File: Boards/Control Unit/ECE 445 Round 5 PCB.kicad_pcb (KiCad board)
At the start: 2 copper layers, 92.1 x 90 mm, 48 parts, among them J1 Screw_Terminal_01x12, J10 Screw_Terminal_01x03, J11 Screw_Terminal_01x12, J12 Screw_Terminal_01x03, J13 Screw_Terminal_01x03, J14 Screw_Terminal_01x03, J15 Screw_Terminal_01x03, J16 Screw_Terminal_01x03, J17 Screw_Terminal_01x03, J18 Screw_Terminal_01x03, J19 Screw_Terminal_01x03, J20 Conn_ARM_JTAG_SWD_10, J27 Screw_Terminal_01x12, J28 Screw_Terminal_01x12, J3 Screw_Terminal_01x03, J4 Screw_Terminal_01x03, J5 Screw_Terminal_01x03, J6 Screw_Terminal_01x03, J7 Conn_02x03_Odd_Even, J9 Screw_Terminal_01x03, Q1 NMOS, Q10 NMOS, Q11 NMOS, Q12 NMOS, Q2 NMOS, Q3 NMOS, Q4 NMOS, Q5 NMOS, Q6 NMOS, Q7 NMOS, Q8 NMOS, Q9 NMOS, SW1 SW_Push, U1 STM32F401RBTx

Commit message: Add files via upload
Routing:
- net /Radar_Read: track 0.00 -> 20.4 mm, vias 0 -> 2
- net /H4: track 50.3 -> 44.1 mm, vias 0 -> 2
- net /bigmotor: track 0.00 -> 3.10 mm, vias 0 -> 1
- net /H7: track 17.3 -> 18.0 mm
- net /H8: track 19.2 -> 20.0 mm
- net /JTDI: track 23.7 -> 24.5 mm

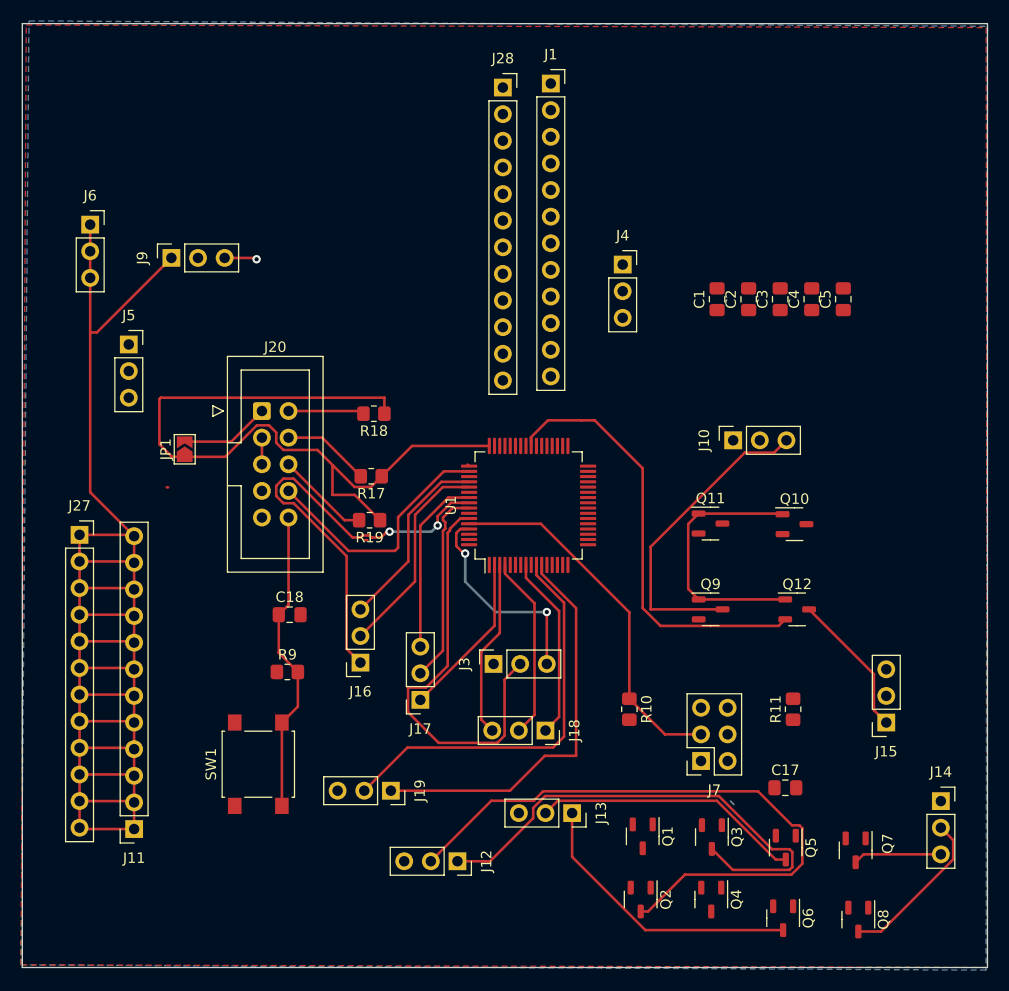
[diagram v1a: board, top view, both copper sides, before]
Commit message: removed extranious 5v power buses
hall effect module is pretty nice
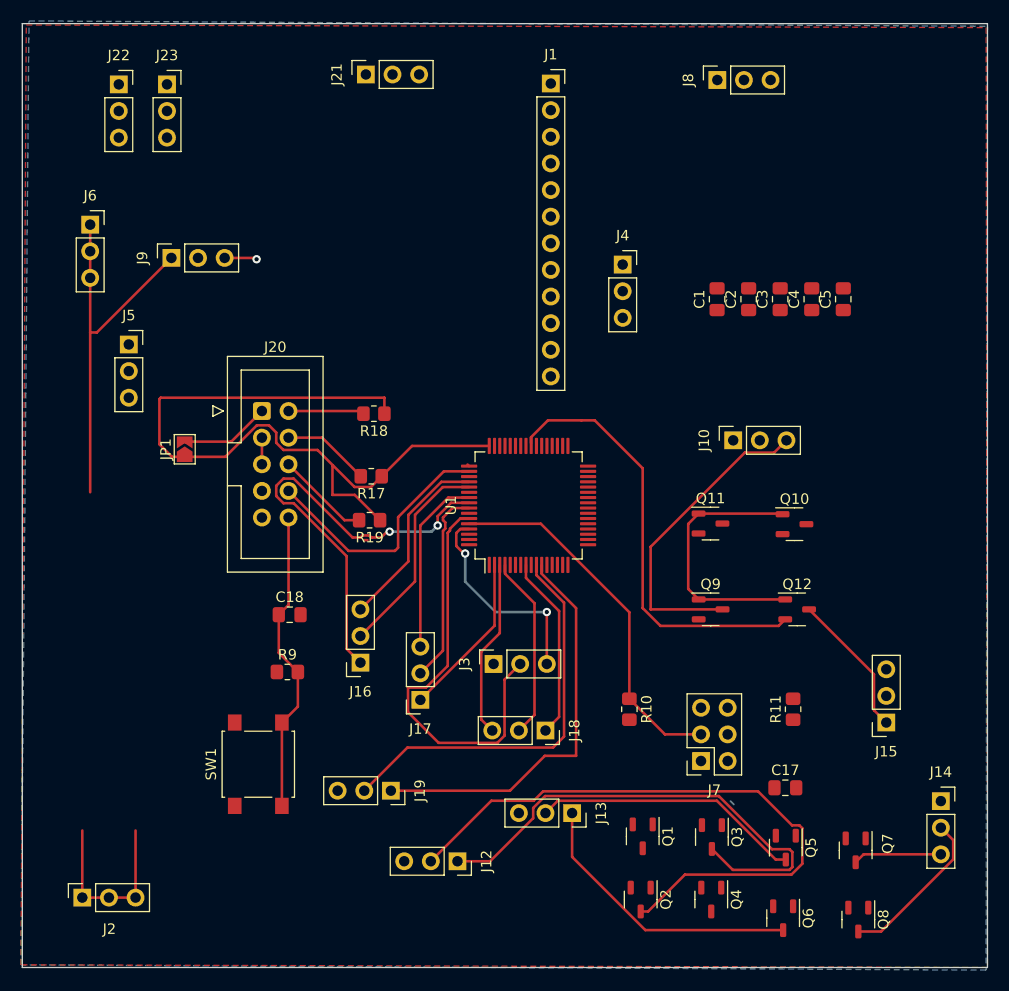
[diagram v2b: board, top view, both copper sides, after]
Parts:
- removed J11, J27, J28: Screw_Terminal_01x12, Connector_PinSocket_2.54mm:PinSocket_1x12_P2.54mm_Vertical
- added J2: Screw_Terminal_01x03, Connector_PinSocket_2.54mm:PinSocket_1x03_P2.54mm_Vertical, F.Cu at (105.4, 123.0)
- added J21: Screw_Terminal_01x03, Connector_PinSocket_2.54mm:PinSocket_1x03_P2.54mm_Vertical, F.Cu at (132.5, 44.5)
- added J22: Screw_Terminal_01x03, Connector_PinSocket_2.54mm:PinSocket_1x03_P2.54mm_Vertical, F.Cu at (108.9, 45.4)
- added J23: Screw_Terminal_01x03, Connector_PinSocket_2.54mm:PinSocket_1x03_P2.54mm_Vertical, F.Cu at (113.5, 45.4)
- added J8: Screw_Terminal_01x03, Connector_PinSocket_2.54mm:PinSocket_1x03_P2.54mm_Vertical, F.Cu at (166.0, 45.0)
- C18: value 1u -> 1uF
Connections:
- U1 pad 40: /T11 -> unconnected-(U1-PC9-Pad40)
- U1 pad 44: /D- -> /T11
- U1 pad 45: /D+ -> unconnected-(U1-PA12-Pad45)
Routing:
- net +5V: track 161.1 -> 54.1 mm

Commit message: routed except gnd and vcc
that was rough
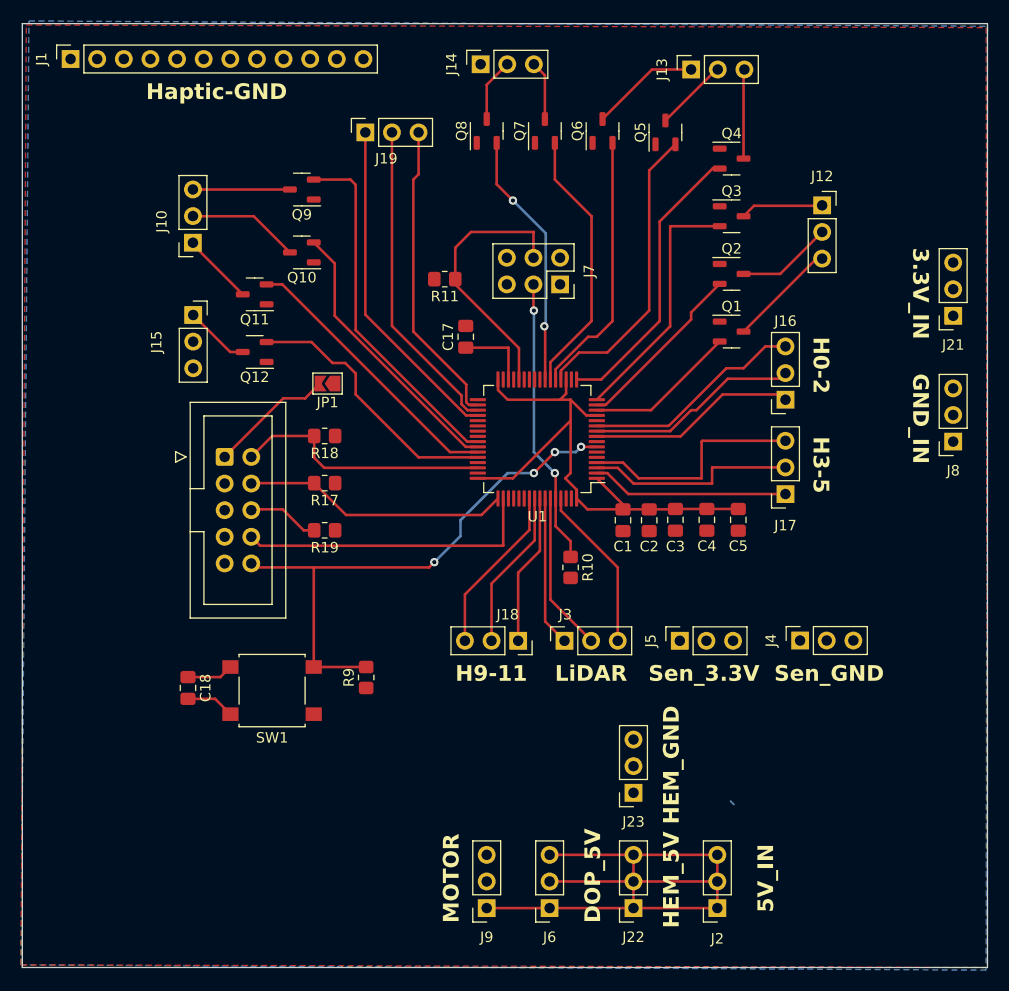
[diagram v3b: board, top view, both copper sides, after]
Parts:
- moved J22 92.7 mm to (158.0, 124.0), turned to 180 degrees
- moved Q8 83.2 mm to (144.0, 49.9), turned to 90 degrees
- moved J14 82.9 mm to (143.4, 43.5), turned to 90 degrees
- moved J23 80.9 mm to (158.0, 113.0), turned to 180 degrees
- moved J6 78.6 mm to (150.0, 124.0), turned to 180 degrees
- moved Q6 77.1 mm to (155.1, 49.9), turned to 90 degrees
- moved J15 76.7 mm to (116.0, 67.4), turned to 0 degrees
- moved Q7 74.8 mm to (149.6, 49.9), turned to 90 degrees
- moved J13 71.8 mm to (163.5, 44.0), turned to 90 degrees
- moved J12 71.6 mm to (176.0, 57.0), turned to 0 degrees
- moved Q4 70.7 mm to (167.4, 52.5), turned to 0 degrees
- moved Q5 69.2 mm to (161.1, 50.0), turned to 90 degrees
- moved J9 68.9 mm to (144.0, 124.0), turned to 180 degrees
- moved J19 62.8 mm to (132.4, 50.0), turned to 90 degrees
- moved J2 60.6 mm to (166.0, 124.0), turned to 180 degrees
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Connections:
- J16 pad 1: /H4 -> /H2
- J16 pad 2: /H8 -> /H1
- J16 pad 3: /H7 -> /H0
- J17 pad 1: /H10 -> /H5
- J17 pad 2: /H5 -> /H4
- J17 pad 3: /H6 -> /H3
- J18 pad 1: /H0 -> /H11
- J18 pad 2: /H9 -> /H10
- J18 pad 3: /H11 -> /H9
- J19 pad 1: /H3 -> /H8
- J19 pad 2: /H2 -> /H7
- J19 pad 3: /H1 -> /H6
- U1 pad 10: /H2 -> /H1
- U1 pad 11: /H3 -> /H0
- U1 pad 2: /H10 -> /H5
- U1 pad 3: /H11 -> /H4
- U1 pad 34: unconnected-(U1-PB13-Pad34) -> /H6
- U1 pad 35: unconnected-(U1-PB14-Pad35) -> /H7
- U1 pad 36: unconnected-(U1-PB15-Pad36) -> /H8
- U1 pad 4: /H9 -> /H3
- U1 pad 52: /H7 -> unconnected-(U1-PC11-Pad52)
- U1 pad 53: /H8 -> unconnected-(U1-PC12-Pad53)
- U1 pad 55: /H6 -> /H9
- U1 pad 56: /H4 -> /H10
- U1 pad 57: /H5 -> /H11
- U1 pad 8: /H0 -> unconnected-(U1-PC0-Pad8)
- U1 pad 9: /H1 -> /H2
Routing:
- net /M1: track 60.4 -> 9.16 mm
- net +3.3V: track 99.3 -> 55.1 mm
- net /M2: track 47.4 -> 7.93 mm
- net /T8: track 0.00 -> 34.1 mm
- net /T4: track 0.00 -> 28.5 mm
- net /NRST: track 29.3 -> 57.7 mm, vias 0 -> 4
- net /T3: track 0.00 -> 27.6 mm
- net /T10: track 0.00 -> 26.8 mm
- net /T9: track 0.00 -> 26.7 mm
- net BOOT1: track 0.00 -> 25.7 mm
- net /T6: track 0.00 -> 25.7 mm
- net /I2C1_SDA: track 40.5 -> 15.2 mm
- net /T5: track 0.00 -> 25.3 mm
- net /T7: track 0.00 -> 24.6 mm, vias 0 -> 2
- net /T2: track 0.00 -> 24.1 mm
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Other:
- board text added: "3.3V_IN"
- board text added: "5V_IN"
- board text added: "DOP_5V"
- board text added: "GND_IN"
- board text added: "H0-2"
- board text added: "H3-5"
- board text added: "H9-11"
- board text added: "HEM_5V"
- board text added: "HEM_GND"
- board text added: "Haptic-GND"
- board text added: "LiDAR"
- board text added: "MOTOR"
- board text added: "Sen_3.3V"
- board text added: "Sen_GND"

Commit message: power routing example
oop
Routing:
- net +3.3V: track 55.1 -> 147.0 mm, vias 0 -> 4
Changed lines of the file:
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@@
     (property "ki_keywords" "transistor NMOS N-MOS N-MOSFET simulation")
     (attr smd)
-    (fp_text reference "Q2" (at 0 -2.4) (layer "F.SilkS")
+    (fp_text reference "Q2" (at -3.3625 -0.5) (layer "F.SilkS")
         (effects (font (size 1 1) (thickness 0.15)))
     )
@@
     (property "ki_keywords" "transistor NMOS N-MOS N-MOSFET simulation")
     (attr smd)
-    (fp_text reference "Q1" (at 0 -2.4) (layer "F.SilkS")
+    (fp_text reference "Q1" (at -3.3625 0) (layer "F.SilkS")
         (effects (font (size 1 1) (thickness 0.15)))
     )
@@
   (segment (start 157 85.9625) (end 153.6125 85.9625) (width 0.25) (layer "F.Cu") (net 3))
   (segment (start 146 75.5) (end 151 75.5) (width 0.25) (layer "F.Cu") (net 3))
+  (segment (start 179.5 87.5) (end 176.575 90.425) (width 0.25) (layer "F.Cu") (net 3))
   (segment (start 153.6125 85.9625) (end 152.575 84.925) (width 0.25) (layer "F.Cu") (net 3))
   (segment (start 151 75.5) (end 152 75.5) (width 0.25) (layer "F.Cu") (net 3))
   (segment (start 162 85.925) (end 165 85.925) (width 0.25) (layer "F.Cu") (net 3))
+  (segment (start 172.5 90.425) (end 168 85.925) (width 0.25) (layer "F.Cu") (net 3))
+  (segment (start 177.5 66.5) (end 173.5 66.5) (width 0.25) (layer "F.Cu") (net 3))
   (segment (start 157 85.9625) (end 159.5 85.9625) (width 0.25) (layer "F.Cu") (net 3))
   (segment (start 151.492764 83) (end 152 82.492764) (width 0.25) (layer "F.Cu") (net 3))
+  (segment (start 167 61) (end 167 61.775) (width 0.25) (layer "F.Cu") (net 3))
   (segment (start 151 75.5) (end 151.575 74.925) (width 0.25) (layer "F.Cu") (net 3))
+  (segment (start 181.58 62.42) (end 177.5 66.5) (width 0.25) (layer "F.Cu") (net 3))
   (segment (start 152 82.492764) (end 152 75.5) (width 0.25) (layer "F.Cu") (net 3))
+  (segment (start 176.575 90.425) (end 172.5 90.425) (width 0.25) (layer "F.Cu") (net 3))
+  (segment (start 181.58 62.42) (end 181.58 60) (width 0.75) (layer "F.Cu") (net 3))
   (segment (start 161.9625 85.9625) (end 162 85.925) (width 0.25) (layer "F.Cu") (net 3))
+  (segment (start 181.58 60) (end 181.58 56.08) (width 0.75) (layer "F.Cu") (net 3))
   (segment (start 157 85.5) (end 154.5 83) (width 0.25) (layer "F.Cu") (net 3))
+  (segment (start 181.58 56.08) (end 178 52.5) (width 0.75) (layer "F.Cu") (net 3))
+  (segment (start 167 61.775) (end 166.225 62.55) (width 0.25) (layer "F.Cu") (net 3))
   (segment (start 165 85.925) (end 168 85.925) (width 0.25) (layer "F.Cu") (net 3))
   (segment (start 145.075 74.575) (end 146 75.5) (width 0.25) (layer "F.Cu") (net 3))
   (segment (start 153.5 77) (end 154.5 77) (width 0.25) (layer "F.Cu") (net 3))
+  (segment (start 166.5 67.775) (end 166.225 68.05) (width 0.25) (layer "F.Cu") (net 3))
+  (segment (start 179.5 76.5) (end 179.5 87.5) (width 0.25) (layer "F.Cu") (net 3))
+  (segment (start 181.58 60) (end 179.5 60) (width 0.25) (layer "F.Cu") (net 3))
   (segment (start 146.5 83) (end 152 77.5) (width 0.25) (layer "F.Cu") (net 3))
+  (segment (start 188.5 62.42) (end 181.58 62.42) (width 0.75) (layer "F.Cu") (net 3))
+  (segment (start 188.5 67.5) (end 179.5 76.5) (width 0.25) (layer "F.Cu") (net 3))
   (segment (start 143.15 83) (end 146.5 83) (width 0.25) (layer "F.Cu") (net 3))
+  (segment (start 166.5 66.5) (end 166.5 67.775) (width 0.25) (layer "F.Cu") (net 3))
   (segment (start 145.075 73.575) (end 145.075 74.575) (width 0.25) (layer "F.Cu") (net 3))
   (segment (start 159.5 85.9625) (end 161.9625 85.9625) (width 0.25) (layer "F.Cu") (net 3))
   (segment (start 157 85.9625) (end 157 85.5) (width 0.25) (layer "F.Cu") (net 3))
   (segment (start 152.575 84.082236) (end 152.575 84.925) (width 0.25) (layer "F.Cu") (net 3))
+  (via (at 167 61) (size 0.8) (drill 0.4) (layers "F.Cu" "B.Cu") (net 3))
+  (via (at 166.5 66.5) (size 0.8) (drill 0.4) (layers "F.Cu" "B.Cu") (net 3))
+  (via (at 179.5 60) (size 0.8) (drill 0.4) (layers "F.Cu" "B.Cu") (net 3))
+  (via (at 173.5 66.5) (size 0.8) (drill 0.4) (layers "F.Cu" "B.Cu") (net 3))
+  (segment (start 178.825 60.675) (end 167.325 60.675) (width 0.25) (layer "B.Cu") (net 3))
+  (segment (start 173.5 66.5) (end 166.5 66.5) (width 0.25) (layer "B.Cu") (net 3))
+  (segment (start 179.5 60) (end 178.825 60.675) (width 0.25) (layer "B.Cu") (net 3))
   (segment locked (start 167.256788 113.794468) (end 167.57232 114.11) (width 0.175) (layer "B.Cu") (net 3))
+  (segment (start 167.325 60.675) (end 167 61) (width 0.25) (layer "B.Cu") (net 3))
   (segment (start 146.075 70.5375) (end 142 70.5375) (width 0.25) (layer "F.Cu") (net 4))
   (segment (start 146.075 73.575) (end 146.075 70.5375) (width 0.25) (layer "F.Cu") (net 4))

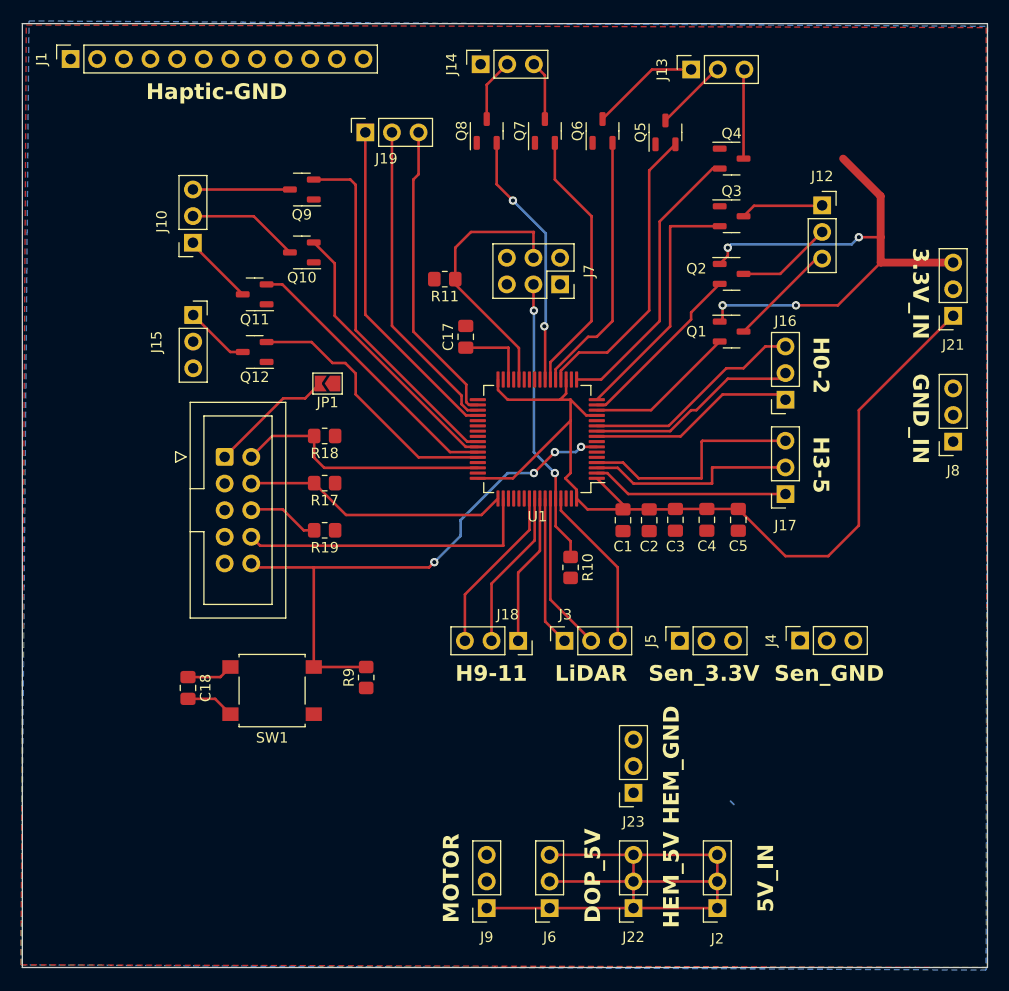
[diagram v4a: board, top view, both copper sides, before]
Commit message: current control unit
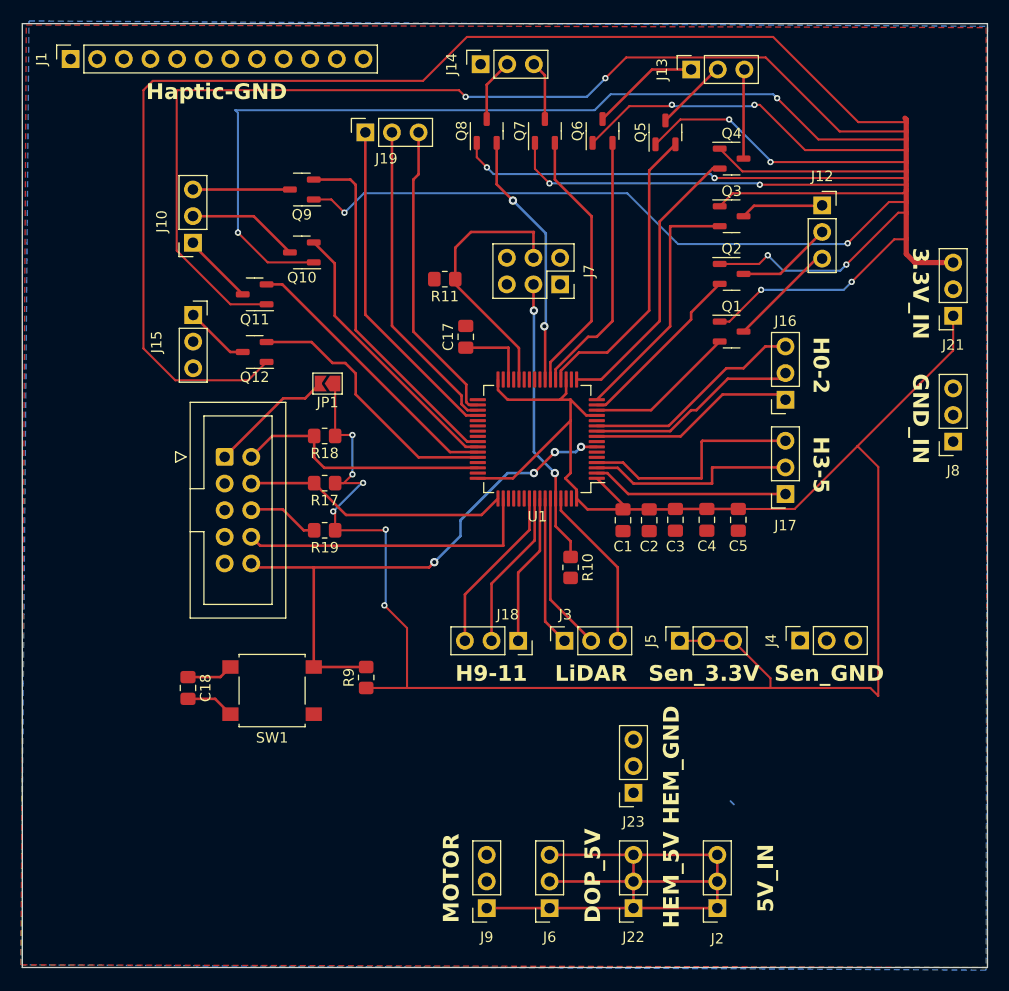
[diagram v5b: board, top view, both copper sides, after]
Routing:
- net +3.3V: track 147.0 -> 815.8 mm, vias 4 -> 24

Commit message: didnt save,
sad
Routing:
- net GND: track 4.66 -> 51.5 mm, vias 0 -> 7
- net /bigmotor: track 0.00 -> 39.3 mm, vias 0 -> 2
- net +3.3V: track 815.8 -> 830.9 mm
- net /NRST: track 57.7 -> 65.7 mm
